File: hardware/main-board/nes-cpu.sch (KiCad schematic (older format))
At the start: 36 parts, among them SW1 NES Reset, U10 74HCT00, U11 PCA9564, U3 74LVC1404, U4 RP2A03, U5 74HCT138, U6 LM4889, U7 AS6C6264, U8 MCP40D17, U9 AT28C64B, Y1 21.5 MHz

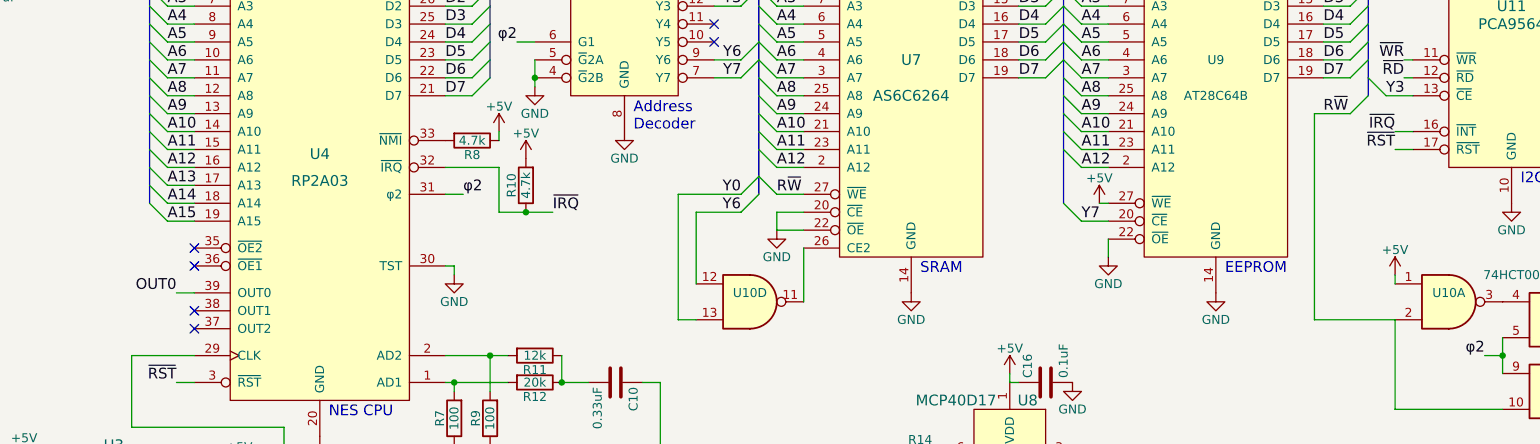
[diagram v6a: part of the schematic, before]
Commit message: Route the OUT1 line from the RP2A03 to the PCA9564's reset pin
This change gives the NES CPU control over resetting its I2C controller,
for improved error recovery and more predictable startup behavior. Also
added a pull-up resistor, similar to how OUT0 was wired, for a more
predictable "high" voltage.

Fixes #8
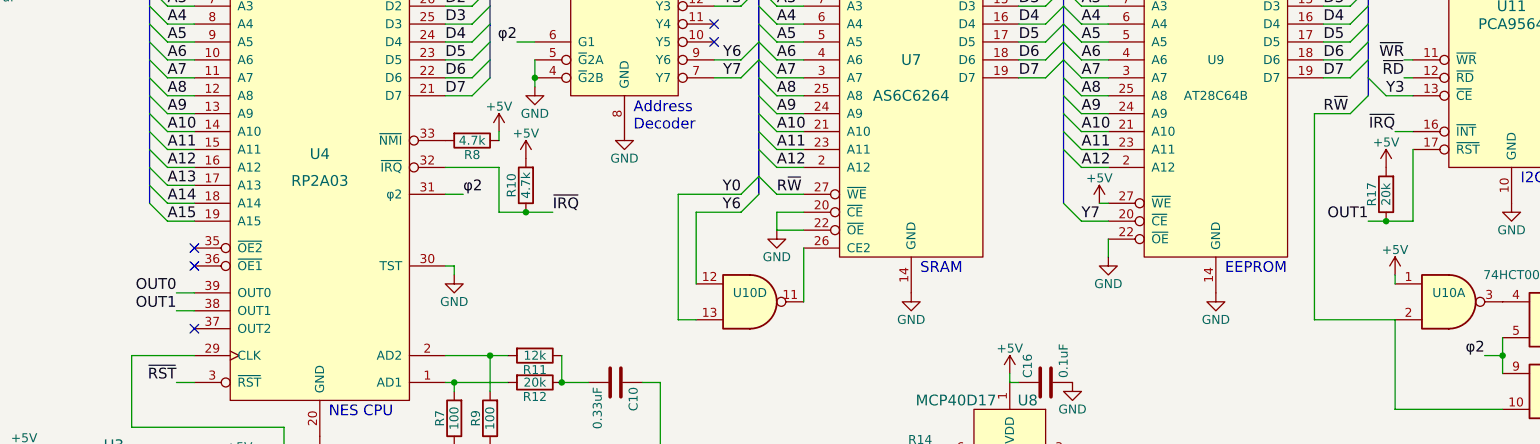
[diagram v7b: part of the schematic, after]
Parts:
- added R17: 20k, Resistor_SMD:R_0805_2012Metric, symbol R
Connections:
- net +5V: now also R17.2
- net ~RST: no longer U11.17 (~RST)
- net OUT1: now reaches U4.38 (OUT1)
- net OUT1: now also U11.17 (~RST), R17.1
- no-connect marks 8 -> 7
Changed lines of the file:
@@
 $EndComp
 $Comp
-L GND #PWR031
+L GND #PWR030
 U 1 1 5A482A78
 P 5500 2700
-F 0 "#PWR031" H 5500 2450 50  0001 C CNN
+F 0 "#PWR030" H 5500 2450 50  0001 C CNN
 F 1 "GND" H 5500 2550 50  0000 C CNN
 F 2 "" H 5500 2700 50  0001 C CNN
@@
 $EndComp
 $Comp
-L GND #PWR032
+L GND #PWR031
 U 1 1 5A482B38
 P 7350 2850
-F 0 "#PWR032" H 7350 2600 50  0001 C CNN
+F 0 "#PWR031" H 7350 2600 50  0001 C CNN
 F 1 "GND" H 7350 2700 50  0000 C CNN
 F 2 "" H 7350 2850 50  0001 C CNN
@@
 $EndComp
 $Comp
-L GND #PWR033
+L GND #PWR032
 U 1 1 5A482F45
 P 3700 2950
-F 0 "#PWR033" H 3700 2700 50  0001 C CNN
+F 0 "#PWR032" H 3700 2700 50  0001 C CNN
 F 1 "GND" H 3700 2800 50  0000 C CNN
 F 2 "" H 3700 2950 50  0001 C CNN
@@
 $EndComp
 $Comp
-L +5V #PWR034
+L +5V #PWR033
 U 1 1 5A483009
 P 3950 2150
-F 0 "#PWR034" H 3950 2000 50  0001 C CNN
+F 0 "#PWR033" H 3950 2000 50  0001 C CNN
 F 1 "+5V" H 3950 2290 50  0000 C CNN
 F 2 "" H 3950 2150 50  0001 C CNN
@@
 $EndComp
 $Comp
-L GND #PWR035
+L GND #PWR034
 U 1 1 5A484C55
 P 750 1550
-F 0 "#PWR035" H 750 1300 50  0001 C CNN
+F 0 "#PWR034" H 750 1300 50  0001 C CNN
 F 1 "GND" H 750 1400 50  0000 C CNN
 F 2 "" H 750 1550 50  0001 C CNN
@@
 $EndComp
 $Comp
-L GND #PWR036
+L GND #PWR035
 U 1 1 5A48770F
 P 3800 3950
-F 0 "#PWR036" H 3800 3700 50  0001 C CNN
+F 0 "#PWR035" H 3800 3700 50  0001 C CNN
 F 1 "GND" H 3800 3800 50  0000 C CNN
 F 2 "" H 3800 3950 50  0001 C CNN
@@
 $EndComp
 $Comp
-L +5V #PWR037
+L +5V #PWR036
 U 1 1 5A4A80C4
 P 7300 2550
-F 0 "#PWR037" H 7300 2400 50  0001 C CNN
+F 0 "#PWR036" H 7300 2400 50  0001 C CNN
 F 1 "+5V" H 7300 2690 50  0000 C CNN
 F 2 "" H 7300 2550 50  0001 C CNN
@@
 $EndComp
 $Comp
-L GND #PWR038
+L GND #PWR037
 U 1 1 5A535823
 P 5300 5300
-F 0 "#PWR038" H 5300 5050 50  0001 C CNN
+F 0 "#PWR037" H 5300 5050 50  0001 C CNN
 F 1 "GND" H 5300 5150 50  0000 C CNN
 F 2 "" H 5300 5300 50  0001 C CNN
@@
 $EndComp
 $Comp
-L +5V #PWR039
+L +5V #PWR038
 U 1 1 5A537858
 P 5900 4450
-F 0 "#PWR039" H 5900 4300 50  0001 C CNN
+F 0 "#PWR038" H 5900 4300 50  0001 C CNN
 F 1 "+5V" H 5900 4590 50  0000 C CNN
 F 2 "" H 5900 4450 50  0001 C CNN
@@
 $EndComp
 $Comp
-L GND #PWR040
+L GND #PWR039
 U 1 1 5A5379A4
 P 5900 5300
-F 0 "#PWR040" H 5900 5050 50  0001 C CNN
+F 0 "#PWR039" H 5900 5050 50  0001 C CNN
 F 1 "GND" H 5900 5150 50  0000 C CNN
 F 2 "" H 5900 5300 50  0001 C CNN
@@
 $EndComp
 $Comp
-L GND #PWR041
+L GND #PWR040
 U 1 1 5A537C65
 P 6300 4500
-F 0 "#PWR041" H 6300 4250 50  0001 C CNN
+F 0 "#PWR040" H 6300 4250 50  0001 C CNN
 F 1 "GND" H 6300 4350 50  0000 C CNN
 F 2 "" H 6300 4500 50  0001 C CNN
@@
 $EndComp
 $Comp
-L +5V #PWR042
+L +5V #PWR041
 U 1 1 5A53B8FF
 P 5050 5050
-F 0 "#PWR042" H 5050 4900 50  0001 C CNN
+F 0 "#PWR041" H 5050 4900 50  0001 C CNN
 F 1 "+5V" H 5050 5190 50  0000 C CNN
 F 2 "" H 5050 5050 50  0001 C CNN
@@
 $EndComp
 $Comp
-L GND #PWR043
+L GND #PWR042
 U 1 1 5A54B775
 P 9950 850
-F 0 "#PWR043" H 9950 600 50  0001 C CNN
+F 0 "#PWR042" H 9950 600 50  0001 C CNN
 F 1 "GND" H 9950 700 50  0000 C CNN
 F 2 "" H 9950 850 50  0001 C CNN
@@
 $EndComp
 $Comp
-L GND #PWR044
+L GND #PWR043
 U 1 1 5A54CD4E
 P 9600 2550
-F 0 "#PWR044" H 9600 2300 50  0001 C CNN
+F 0 "#PWR043" H 9600 2300 50  0001 C CNN
 F 1 "GND" H 9600 2400 50  0000 C CNN
 F 2 "" H 9600 2550 50  0001 C CNN
@@
 $EndComp
 $Comp
-L GND #PWR045
+L GND #PWR044
 U 1 1 5A544BC2
 P 9850 6100
-F 0 "#PWR045" H 9850 5850 50  0001 C CNN
+F 0 "#PWR044" H 9850 5850 50  0001 C CNN
 F 1 "GND" H 9850 5950 50  0000 C CNN
 F 2 "" H 9850 6100 50  0001 C CNN
@@
 $EndComp
 $Comp
-L +5V #PWR046
+L +5V #PWR045
 U 1 1 5A544C57
 P 9850 5100
-F 0 "#PWR046" H 9850 4950 50  0001 C CNN
+F 0 "#PWR045" H 9850 4950 50  0001 C CNN
 F 1 "+5V" H 9850 5240 50  0000 C CNN
 F 2 "" H 9850 5100 50  0001 C CNN
@@
 $EndComp
 $Comp
-L +5V #PWR047
+L +5V #PWR046
 U 1 1 5A5498C0
 P 8950 2950
-F 0 "#PWR047" H 8950 2800 50  0001 C CNN
+F 0 "#PWR046" H 8950 2800 50  0001 C CNN
 F 1 "+5V" H 8950 3090 50  0000 C CNN
 F 2 "" H 8950 2950 50  0001 C CNN
@@
 $EndComp
 $Comp
-L +5V #PWR048
+L +5V #PWR047
 U 1 1 5A572C0E
 P 4100 2300
-F 0 "#PWR048" H 4100 2150 50  0001 C CNN
+F 0 "#PWR047" H 4100 2150 50  0001 C CNN
 F 1 "+5V" H 4100 2440 50  0000 C CNN
 F 2 "" H 4100 2300 50  0001 C CNN
@@
 $EndComp
 $Comp
-L +3.3V #PWR049
+L +3.3V #PWR048
 U 1 1 5A5AEE39
 P 9600 800
-F 0 "#PWR049" H 9600 650 50  0001 C CNN
+F 0 "#PWR048" H 9600 650 50  0001 C CNN
 F 1 "+3.3V" H 9600 940 50  0000 C CNN
 F 2 "" H 9600 800 50  0001 C CNN
@@
 NoConn ~ 2250 2800
 NoConn ~ 2250 2900
-NoConn ~ 2250 3150
 NoConn ~ 2250 3250
 NoConn ~ 5150 1250
@@
 $EndComp
 $Comp
-L GND #PWR052
+L GND #PWR049
 U 1 1 5A65083D
 P 7150 3550
-F 0 "#PWR052" H 7150 3300 50  0001 C CNN
+F 0 "#PWR049" H 7150 3300 50  0001 C CNN
 F 1 "GND" H 7150 3400 50  0000 C CNN
 F 2 "" H 7150 3550 50  0001 C CNN
@@
 	6800 3550 6850 3550
 $Comp
-L GND #PWR053
+L GND #PWR050
 U 1 1 5A6540A9
 P 6800 4450
-F 0 "#PWR053" H 6800 4200 50  0001 C CNN
+F 0 "#PWR050" H 6800 4200 50  0001 C CNN
 F 1 "GND" H 6800 4300 50  0000 C CNN
 F 2 "" H 6800 4450 50  0001 C CNN
@@
 Wire Wire Line
 	2250 3550 2150 3550
-Text Label 8950 2250 2    60   ~ 0
-~RST
-Wire Wire Line
-	9050 2250 8950 2250
 Text Label 4250 2600 0    60   ~ 0
 ~IRQ
@@
 Reset Button
 $Comp
-L +5V #PWR?
+L +5V #PWR051
 U 1 1 5B2AA23C
 P 6800 3500
-F 0 "#PWR?" H 6800 3350 50  0001 C CNN
+F 0 "#PWR051" H 6800 3350 50  0001 C CNN
 F 1 "+5V" H 6800 3640 50  0000 C CNN
 F 2 "" H 6800 3500 50  0001 C CNN
@@
 Wire Wire Line
 	4950 3200 5050 3200
+$Comp
+L R R17
+U 1 1 5B38A939
+P 8900 2500
+F 0 "R17" V 8980 2500 50  0000 C CNN
+F 1 "20k" V 8900 2500 50  0000 C CNN
+F 2 "Resistor_SMD:R_0805_2012Metric" V 8830 2500 50  0001 C CNN
+F 3 "http://www.vishay.com/docs/20035/dcrcwe3.pdf" H 8900 2500 50  0001 C CNN
+F 4 "RES SMD 20K OHM 5% 1/8W 0805" H 8900 2500 60  0001 C CNN "Description"
+F 5 "Vishay Dale" H 8900 2500 60  0001 C CNN "Manufacturer"
+F 6 "CRCW080520K0JNEA" H 8900 2500 60  0001 C CNN "Manufacturer PN"
+F 7 "Digi-Key" H 8980 2600 50  0001 C CNN "Supplier"
+F 8 "541-20KACT-ND" H 8900 2500 60  0001 C CNN "Supplier PN"
+	1    8900 2500
+	-1   0    0    1
+$EndComp
+$Comp
+L +5V #PWR052
+U 1 1 5B38AA5F
+P 8900 2350
+F 0 "#PWR052" H 8900 2200 50  0001 C CNN
+F 1 "+5V" H 8900 2490 50  0000 C CNN
+F 2 "" H 8900 2350 50  0001 C CNN
+F 3 "" H 8900 2350 50  0001 C CNN
+	1    8900 2350
+	1    0    0    -1
+$EndComp
+Wire Wire Line
+	9050 2650 9050 2250
+Wire Wire Line
+	8800 2650 9050 2650
+Text Label 2150 3150 2    60   ~ 0
+OUT1
+Wire Wire Line
+	2250 3150 2150 3150
+Text Label 8800 2650 2    60   ~ 0
+OUT1
+Connection ~ 8900 2650
 $EndSCHEMATC
